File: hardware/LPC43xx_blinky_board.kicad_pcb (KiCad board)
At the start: 2 copper layers, 58 parts, among them J1 Conn_ARM_JTAG_SWD_10, J2 USB_B_Micro, J3 Micro_SD_Card, SW1 SW_DIP_x01, SW2 SW_DIP_x04, SW3 SW_SPST, SW4 SW_SPST, U1 LPC4337JBD144, U2 SST26VF032B, U3 MCP1825S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

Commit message: Starting layout work for blinky board
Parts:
- added G***: LOGO, Logo:Jitter, F.Cu at (197.8, 71.8)
- added J4: Conn_01x20_Female, Connector_PinSocket_2.54mm:PinSocket_1x20_P2.54mm_Vertical, F.Cu at (133.1, 60.5)
- added J5: Conn_01x04_Male, Connector_PinHeader_2.54mm:PinHeader_1x04_P2.54mm_Horizontal, F.Cu at (115.6, 97.5)
- moved J2 153.7 mm to (114.2, 78.2), turned to 270 degrees
- moved U3 139.3 mm to (124.4, 73.3), turned to 90 degrees
- moved SW1 123.3 mm to (176.2, 66.2)
- moved SW2 120.3 mm to (176.8, 76.2)
- moved J3 119.5 mm to (177.2, 91.5), turned to 90 degrees
- moved D4 84.6 mm to (199.0, 109.0), turned to 90 degrees
- moved SW4 82.8 mm to (173.0, 109.0)
- moved D3 81.7 mm to (196.0, 109.0), turned to 90 degrees
- moved D2 81.4 mm to (193.0, 109.0), turned to 90 degrees
- moved SW3 81.0 mm to (181.8, 109.0)
- moved D1 79.6 mm to (190.0, 109.0), turned to 90 degrees
- moved RN3 77.3 mm to (194.2, 105.0), turned to 90 degrees
- moved C29 74.3 mm to (185.2, 105.8)
- moved Y1 73.3 mm to (151.0, 73.0), turned to 180 degrees
- moved J1 69.6 mm to (123.5, 93.3), turned to 180 degrees
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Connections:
- net Net-(J1-Pad2) renamed /SWDIO
- net Net-(J1-Pad4) renamed /SWDCLK
- Y2 pad 1: Net-(C13-Pad1) -> Net-(C12-Pad1)
- Y2 pad 2: Net-(C12-Pad1) -> Net-(C13-Pad1)
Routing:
- net Net-(J1-Pad6): track 0.00 -> 41.6 mm
- net +3V3: track 0.00 -> 34.0 mm
- net /SWDCLK: track 0.00 -> 28.3 mm
- net /SWDIO: track 0.00 -> 25.5 mm
- net /USB_HS_D+: track 0.00 -> 21.1 mm, vias 0 -> 2
- net Net-(J1-Pad8): track 0.00 -> 20.4 mm
- net /USB_HS_D-: track 0.00 -> 12.0 mm
- net GND: track 0.00 -> 9.60 mm, vias 0 -> 9
- net Net-(C12-Pad1): track 0.00 -> 8.89 mm
- net Net-(C3-Pad2): track 0.00 -> 8.05 mm
- net Net-(C1-Pad1): track 0.00 -> 7.69 mm
- net Net-(L2-Pad1): track 0.00 -> 6.49 mm
- net Net-(C13-Pad1): track 0.00 -> 6.13 mm
- net Net-(C4-Pad2): track 0.00 -> 5.51 mm
- net Net-(R2-Pad1): track 0.00 -> 4.12 mm
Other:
- board outline added: 91 x 55 mm
- net class Default: clearance 0.2 -> 0.15; trace_width 0.25 -> 0.2
- net class Power added: clearance 0.15, trace_width 0.3, via_dia 1, via_drill 0.6
- rule pad_to_mask_clearance: 0.2 -> 0.075
- rule trace_clearance: 0.2 -> 0.15

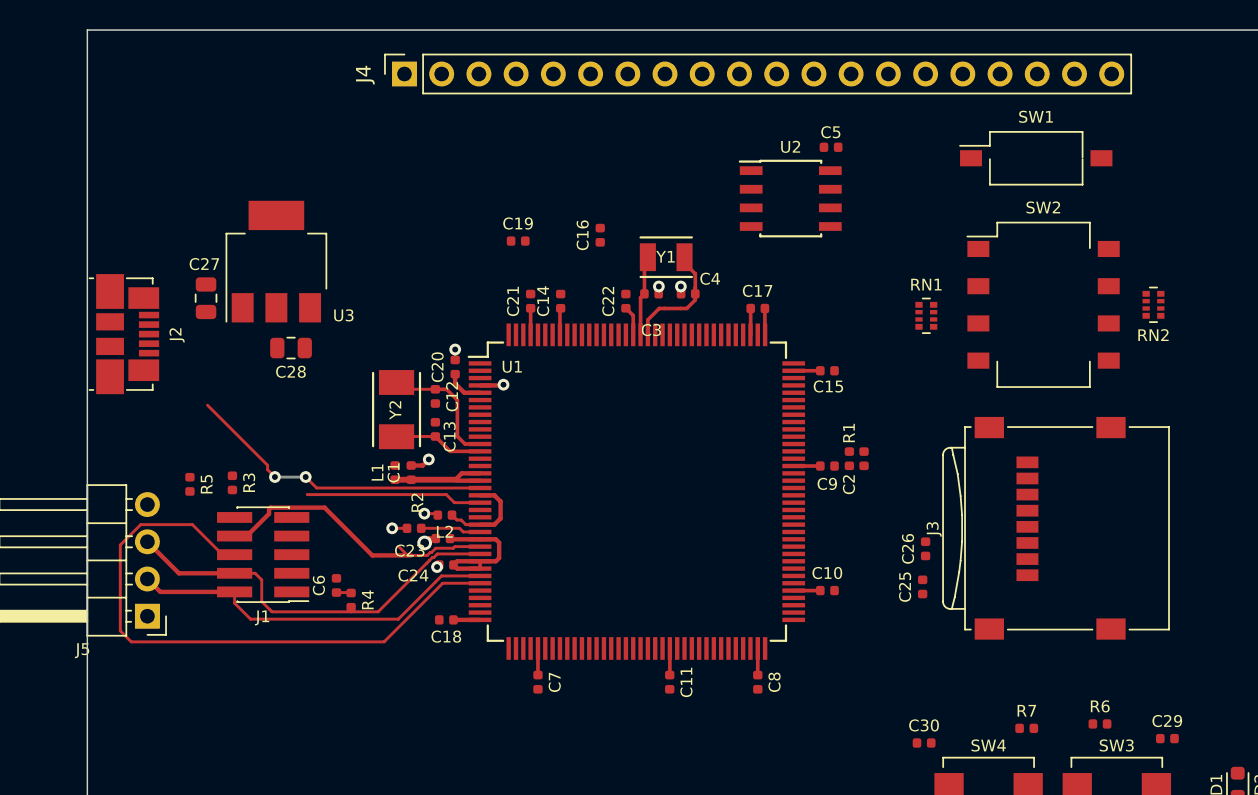
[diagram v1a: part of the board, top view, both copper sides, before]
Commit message: Routed the left side of the board
- USB
- JTAG
- Crystals
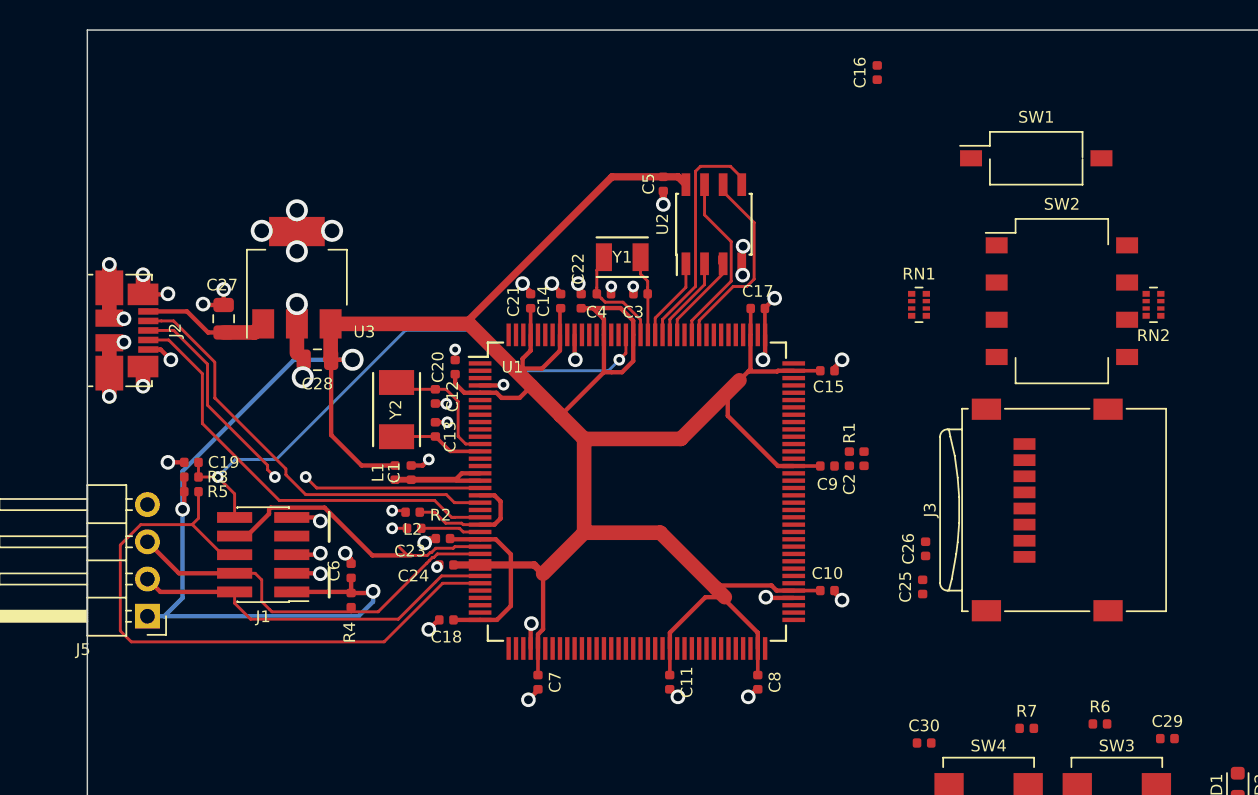
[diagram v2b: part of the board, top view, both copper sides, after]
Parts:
- removed J4: Conn_01x20_Female, Connector_PinSocket_2.54mm:PinSocket_1x20_P2.54mm_Vertical
- moved C19 26.9 mm to (118.6, 87.0), turned to 180 degrees
- moved C16 21.9 mm to (165.4, 60.4)
- moved C5 11.7 mm to (150.8, 68.0), turned to 270 degrees
- moved U2 5.53 mm to (154.2, 70.8), turned to 90 degrees
- moved C3 3.25 mm to (149.2, 75.5)
- moved C4 3.25 mm to (146.8, 75.5)
- moved C22 3.05 mm to (145.2, 76.0)
- moved Y1 3.00 mm to (148.0, 73.0)
- moved R3 2.83 mm to (118.6, 88.0), turned to 0 degrees
- moved L2 2.21 mm to (133.7, 90.4)
- moved C28 1.97 mm to (127.2, 80.0)
- moved C27 1.84 mm to (120.8, 77.2)
- moved U3 1.78 mm to (125.8, 74.4)
- moved C6 1.41 mm to (129.5, 94.4)
- moved SW2 1.27 mm to (178.0, 76.0)
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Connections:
- J2 pad 4: Net-(J2-Pad4) -> /USB_ID
- U1 pad 104: Net-(U1-Pad104) -> /LED_YELLOW
- U1 pad 105: Net-(U1-Pad105) -> /LED_BLUE
- U1 pad 106: Net-(U1-Pad106) -> /LED_GREEN
- U1 pad 108: Net-(U1-Pad108) -> /LED_RED
- U1 pad 22: Net-(U1-Pad22) -> /USB_ID
- U1 pad 73: /LED_YELLOW -> Net-(U1-Pad73)
- U1 pad 74: /LED_BLUE -> Net-(U1-Pad74)
- U1 pad 78: /LED_GREEN -> Net-(U1-Pad78)
- U1 pad 79: /LED_RED -> Net-(U1-Pad79)
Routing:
- net +3V3: track 34.0 -> 241.9 mm, vias 0 -> 3
- net GND: track 9.60 -> 69.7 mm, vias 9 -> 49
- net /~RESET: track 0.00 -> 40.4 mm, vias 0 -> 2
- net /USB_ID: track 0.00 -> 29.6 mm
- net /USB_HS_D-: track 12.0 -> 29.4 mm
- net /SPIFI_MOSI: track 0.00 -> 16.2 mm
- net /SPIFI_SCK: track 0.00 -> 13.2 mm
- net /SPIFI_SIO3: track 0.00 -> 12.1 mm
- net VBUS: track 0.00 -> 8.68 mm
- net /USB_HS_D+: track 21.1 -> 28.9 mm
- net /SPIFI_SIO2: track 0.00 -> 7.10 mm
- net /SPIFI_MISO: track 0.00 -> 5.83 mm
- net /SPIFI_CS: track 0.00 -> 5.72 mm
- net Net-(C3-Pad2): track 8.05 -> 5.51 mm
- net Net-(J1-Pad6): track 41.6 -> 44.0 mm
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- added copper zone on Ground, net GND
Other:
- copper layers 2 -> 4
- board text added: "Connector Clearance"

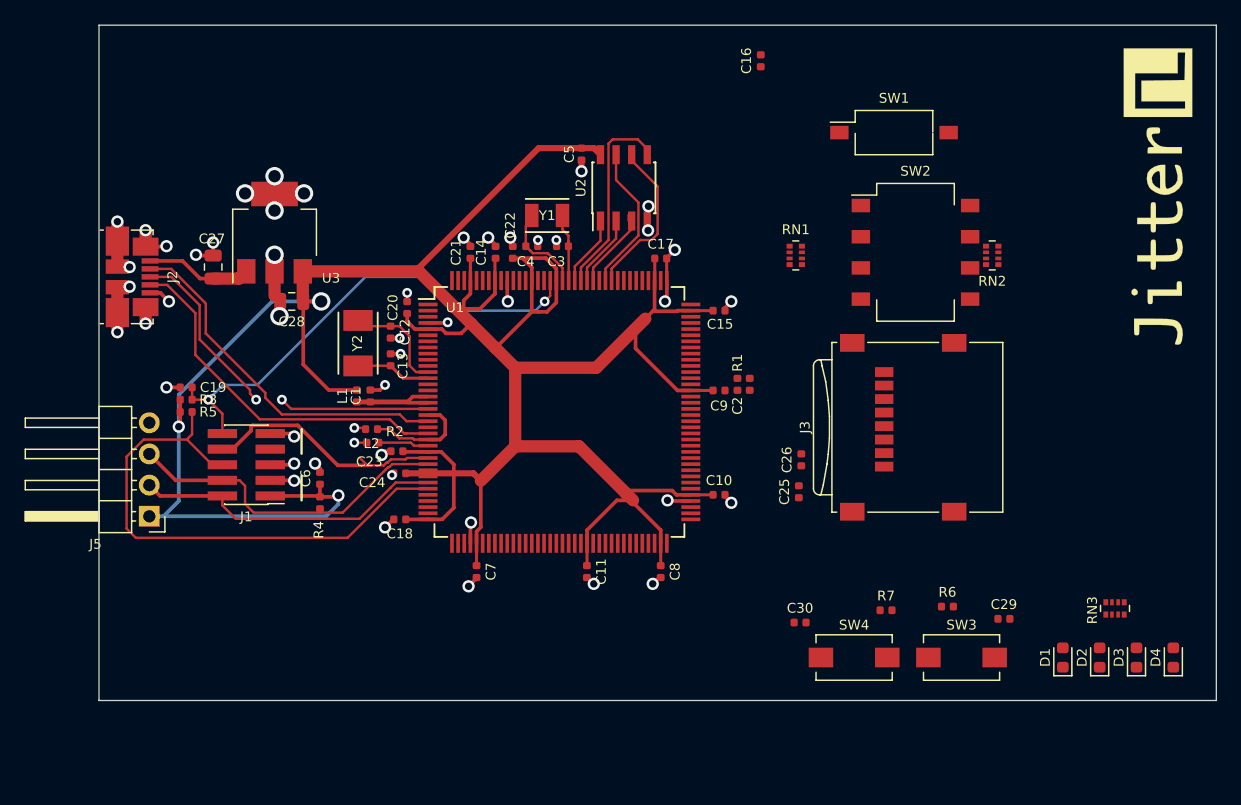
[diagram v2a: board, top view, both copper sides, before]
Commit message: Finish routing except random IO headers
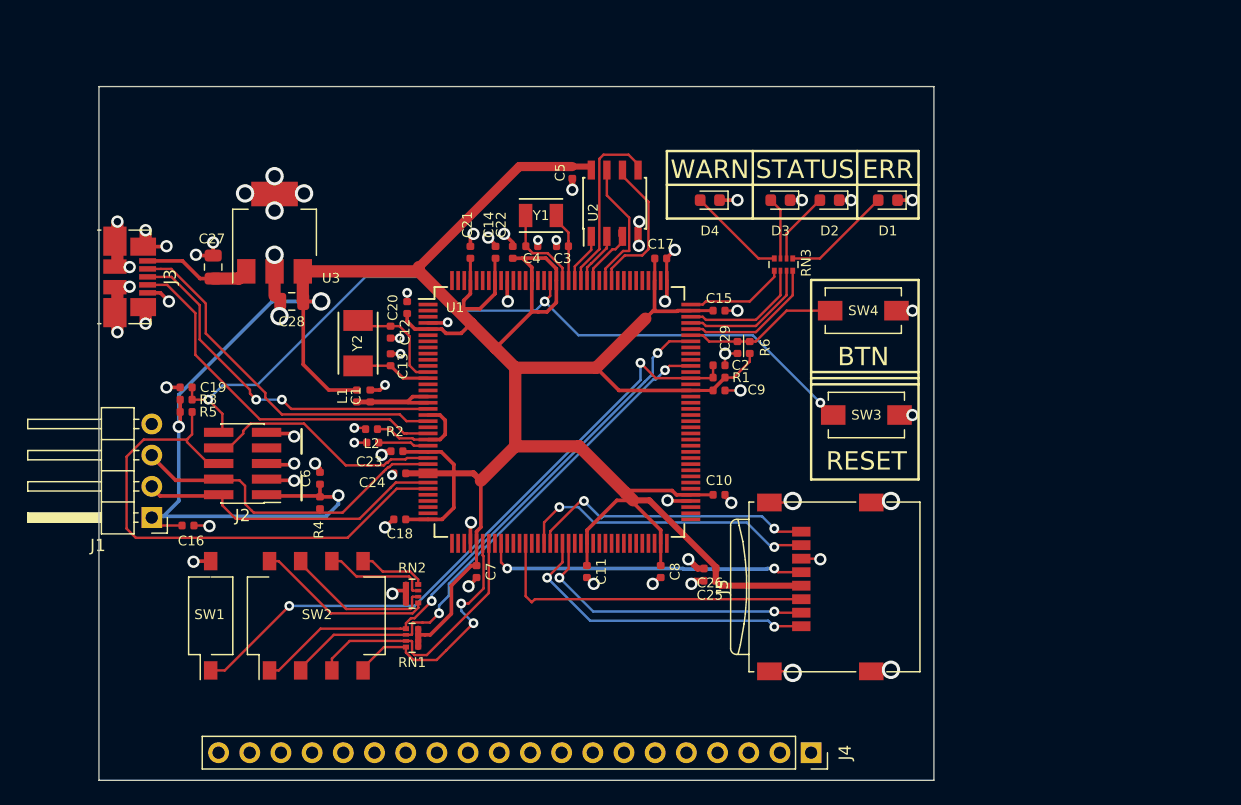
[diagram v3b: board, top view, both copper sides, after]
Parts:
- removed C30: 100nF, Capacitor_SMD:C_0402_1005Metric
- removed G***: LOGO, Logo:Jitter
- removed R7: 100k, Resistor_SMD:R_0402_1005Metric
- added J4: Conn_01x20_Female, Connector_PinSocket_2.54mm:PinSocket_1x20_P2.54mm_Vertical, F.Cu at (169.5, 116.8)
- J1: value Conn_ARM_JTAG_SWD_10 -> Conn_01x04_Male; footprint Connector_PinHeader_1.27mm:PinHeader_2x05_P1.27mm_Vertical_SMD -> Connector_PinHeader_2.54mm:PinHeader_1x04_P2.54mm_Horizontal
- J2: value USB_B_Micro -> Conn_ARM_JTAG_SWD_10; footprint Connector_USB:USB_Micro-B_Molex_47346-0001 -> Connector_PinHeader_1.27mm:PinHeader_2x05_P1.27mm_Vertical_SMD
- J3: value Micro_SD_Card -> USB_B_Micro; footprint Connector_Card:microSD_HC_Wuerth_693072010801 -> Connector_USB:USB_Micro-B_Molex_47346-0001
- J5: value Conn_01x04_Male -> Micro_SD_Card; footprint Connector_PinHeader_2.54mm:PinHeader_1x04_P2.54mm_Horizontal -> Connector_Card:microSD_HC_Wuerth_693072010801
- moved SW1 68.2 mm to (120.6, 105.6), turned to 90 degrees
- moved J3 64.2 mm to (114.0, 78.0), turned to 270 degrees
- moved C16 60.1 mm to (118.8, 98.2), turned to 0 degrees
- moved SW2 57.1 mm to (129.2, 105.6), turned to 90 degrees
- moved J5 55.0 mm to (170.2, 103.2), turned to 90 degrees
- moved RN2 54.7 mm to (137.0, 103.8), turned to 0 degrees
- moved D4 53.0 mm to (161.2, 71.8), turned to 180 degrees
- moved D3 47.2 mm to (167.0, 71.8), turned to 180 degrees
- moved RN1 44.1 mm to (137.0, 107.4)
- moved D2 43.3 mm to (171.0, 71.8), turned to 180 degrees
- moved D1 39.9 mm to (175.8, 71.8), turned to 180 degrees
- moved RN3 38.9 mm to (167.2, 77.0), turned to 270 degrees
- moved C29 31.0 mm to (163.5, 83.8), turned to 270 degrees
- moved SW4 28.3 mm to (173.8, 80.8)
- moved R6 26.5 mm to (164.5, 83.8), turned to 90 degrees
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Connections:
- C29 pad 1: /~RESET -> /USR_SW
- J1 pad 3: GND -> /SWDCLK
- J1 pad 4: /SWDCLK -> GND
- J2 pad 1: VBUS -> +3V3
- J2 pad 2: /USB_HS_D- -> /SWDIO
- J2 pad 3: /USB_HS_D+ -> GND
- J2 pad 4: /USB_ID -> /SWDCLK
- J2 pad 6: GND -> Net-(J2-Pad6)
- J3 pad 1: /SD_DAT2 -> VBUS
- J3 pad 2: /SD_DAT3 -> /USB_HS_D-
- J3 pad 3: /SD_CMD -> /USB_HS_D+
- J3 pad 4: +3V3 -> /USB_ID
- J3 pad 5: /SD_CLK -> GND
- J5 pad 1: +3V3 -> /SD_DAT2
- J5 pad 2: /SWDIO -> /SD_DAT3
- J5 pad 3: /SWDCLK -> /SD_CMD
- J5 pad 4: GND -> +3V3
- R5 pad 2: Net-(J1-Pad6) -> Net-(J2-Pad6)
- R6 pad 2: /~RESET -> /USR_SW
- RN3 pad 6: /LED_BLUE -> /LED_GREEN
- RN3 pad 7: /LED_GREEN -> /LED_BLUE
- U1 pad 103: Net-(U1-Pad103) -> /USR_SW
- U1 pad 104: /LED_YELLOW -> /LED_RED
- U1 pad 108: /LED_RED -> /LED_YELLOW
- U1 pad 26: Net-(J1-Pad8) -> Net-(J2-Pad8)
- U1 pad 31: Net-(J1-Pad6) -> Net-(J2-Pad6)
- U1 pad 80: /USR_SW -> Net-(U1-Pad80)
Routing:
- net /BOOT_PIN: track 0.00 -> 53.6 mm, vias 0 -> 2
- net /BOOT0: track 0.00 -> 46.8 mm, vias 0 -> 2
- net Net-(J2-Pad6): track 0.00 -> 44.6 mm
- net Net-(J1-Pad6): track 44.0 -> 0.00 mm
- net /BOOT1: track 0.00 -> 43.6 mm, vias 0 -> 2
- net +3V3: track 241.9 -> 275.1 mm
- net GND: track 69.7 -> 97.7 mm, vias 49 -> 67
- net /~RESET: track 40.4 -> 67.8 mm, vias 2 -> 3
- net /SD_CMD: track 0.00 -> 27.1 mm
- net /SD_CLK: track 0.00 -> 26.4 mm, vias 0 -> 2
- net /SD_DAT2: track 0.00 -> 25.7 mm, vias 0 -> 2
- net /SD_DAT0: track 0.00 -> 24.6 mm, vias 0 -> 2
- net /SD_DAT3: track 0.00 -> 24.2 mm, vias 0 -> 2
- net /SD_DAT1: track 0.00 -> 23.6 mm, vias 0 -> 2
- net /BOOT2: track 0.00 -> 21.5 mm
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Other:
- board size 91 x 55 mm -> 68 x 56.5 mm
- board text added: "BTN"
- board text added: "ERR"
- board text added: "RESET"
- board text added: "STATUS"
- board text added: "WARN"

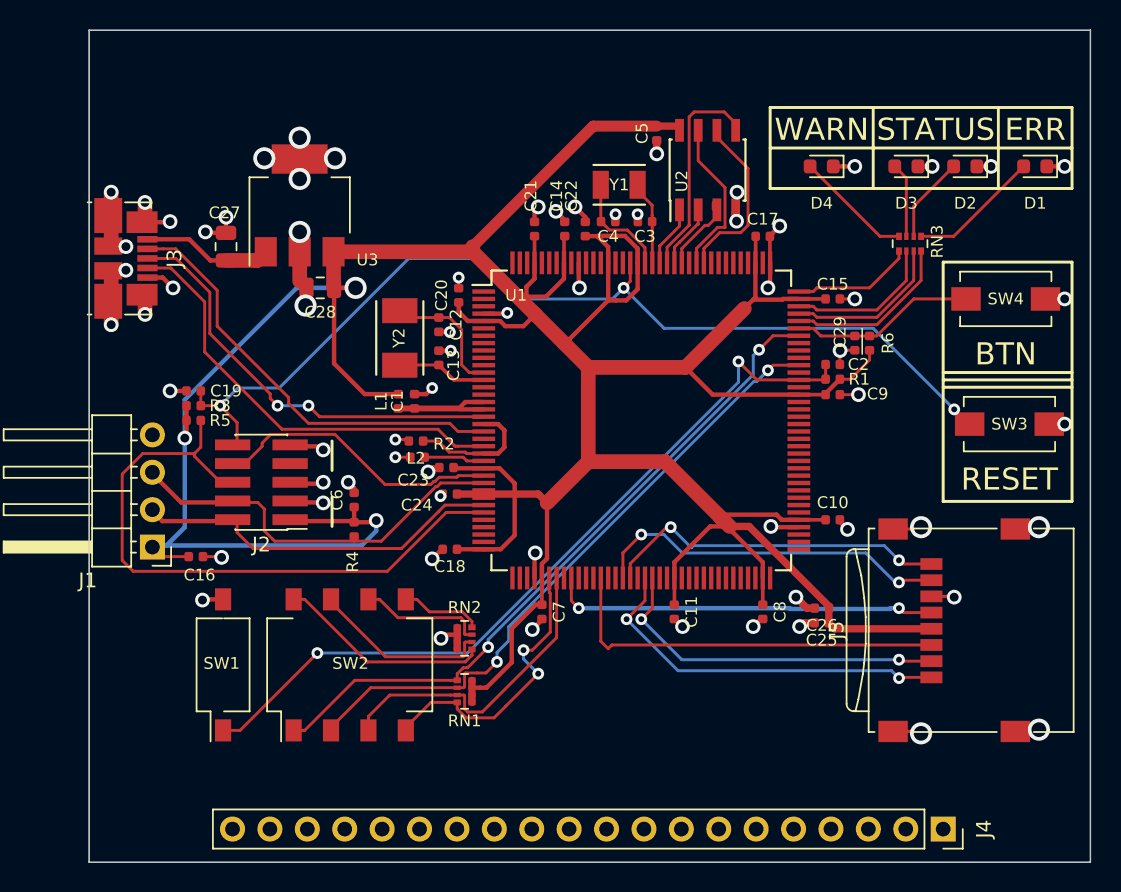
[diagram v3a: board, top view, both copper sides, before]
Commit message: Route all missing connections
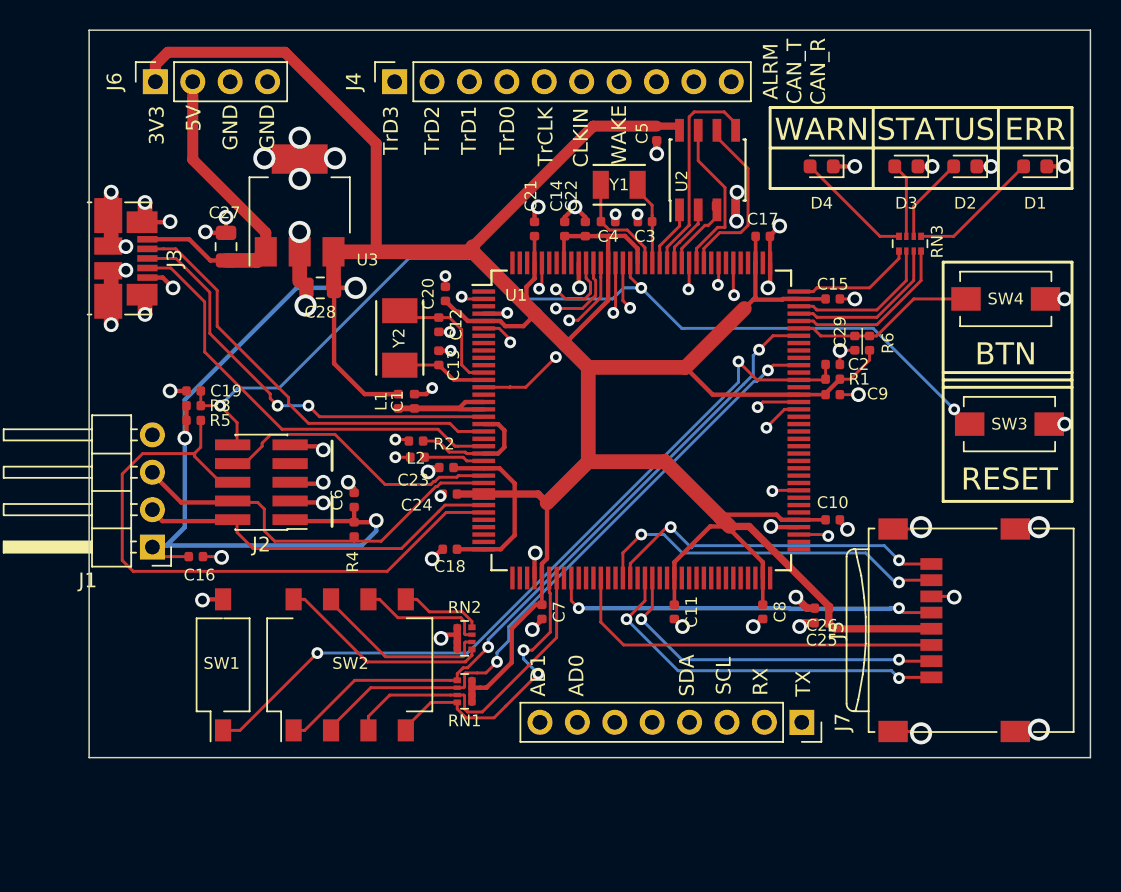
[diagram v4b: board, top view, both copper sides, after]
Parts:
- added J6: Conn_01x04_Female, Connector_PinSocket_2.54mm:PinSocket_1x04_P2.54mm_Vertical, F.Cu at (116.0, 66.0)
- added J7: Conn_01x08_Female, Connector_PinSocket_2.54mm:PinSocket_1x08_P2.54mm_Vertical, F.Cu at (159.9, 109.5)
- J4: footprint Connector_PinSocket_2.54mm:PinSocket_1x20_P2.54mm_Vertical -> Connector_PinSocket_2.54mm:PinSocket_1x10_P2.54mm_Vertical
- moved J4 63.0 mm to (132.2, 66.0), turned to 90 degrees
- moved C20 0.91 mm to (135.7, 80.4)
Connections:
- J4 pad 1: /CAN_RD -> /TRACEDATA3
- J4 pad 10: Net-(J4-Pad10) -> /CAN_RD
- J4 pad 2: /CAN_TD -> /TRACEDATA2
- J4 pad 3: Net-(J4-Pad3) -> /TRACEDATA1
- J4 pad 4: Net-(J4-Pad4) -> /TRACEDATA0
- J4 pad 5: /UART_TX -> /TRACECLK
- J4 pad 6: /UART_RX -> /CLKIN
- J4 pad 7: Net-(J4-Pad7) -> /WAKUP
- J4 pad 8: /AD0 -> /ALARM
- J4 pad 9: /AD1 -> /CAN_TD
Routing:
- net /CLKIN: track 0.00 -> 33.2 mm, vias 0 -> 1
- net /AD1: track 0.00 -> 32.7 mm, vias 0 -> 1
- net /AD0: track 0.00 -> 30.2 mm, vias 0 -> 1
- net /WAKUP: track 0.00 -> 26.5 mm, vias 0 -> 1
- net /SDA: track 0.00 -> 26.3 mm, vias 0 -> 1
- net /ALARM: track 0.00 -> 24.6 mm, vias 0 -> 1
- net /TRACEDATA0: track 0.00 -> 24.3 mm, vias 0 -> 1
- net /SCL: track 0.00 -> 23.8 mm, vias 0 -> 1
- net /TRACEDATA1: track 0.00 -> 23.7 mm, vias 0 -> 1
- net /TRACECLK: track 0.00 -> 22.8 mm, vias 0 -> 1
- net /TRACEDATA2: track 0.00 -> 22.5 mm, vias 0 -> 1
- net /TRACEDATA3: track 0.00 -> 21.0 mm, vias 0 -> 1
- net +3V3: track 275.1 -> 295.0 mm
- net /UART_RX: track 0.00 -> 18.3 mm, vias 0 -> 1
- net /CAN_RD: track 0.00 -> 17.1 mm, vias 0 -> 1
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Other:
- board size 68 x 56.5 mm -> 68 x 49.4 mm
- board text added: "3V3"
- board text added: "5V"
- board text added: "AD0"
- board text added: "AD1"
- board text added: "ALRM CAN_T CAN_R"
- board text added: "CLKIN"
- board text added: "GND"
- board text added: "RX"
- board text added: "SCL"
- board text added: "SDA"
- board text added: "TX"
- board text added: "TrCLK"
- board text added: "TrD0"
- board text added: "TrD1"
- board text added: "TrD2"
- board text added: "TrD3"
- board text added: "WAKE"
